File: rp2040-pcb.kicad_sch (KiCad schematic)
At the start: 43 parts, among them J1 Conn_01x20_Male, J2 Conn_01x20_Male, J3 USB_C_Receptacle, SW1 SW_Push, SW2 SW_Push, U1 TPS54202DDC, U2 W25Q128JVS, U3 RP2040, Y1 Crystal_GND24

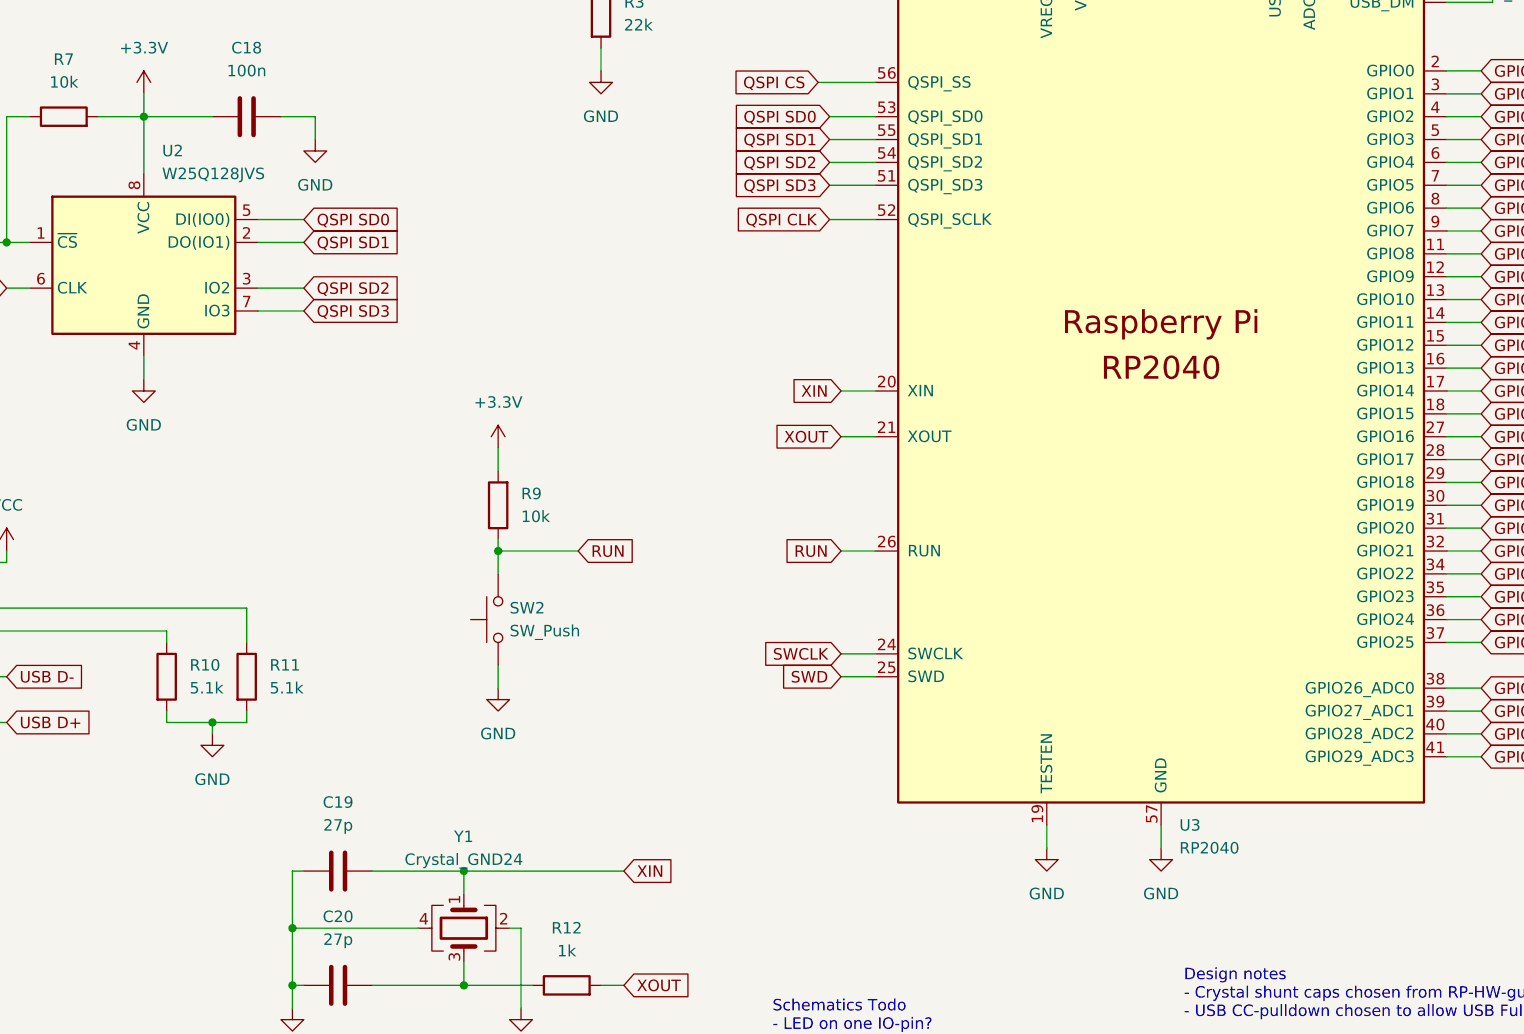
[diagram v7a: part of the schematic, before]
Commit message: Added footprints to all components.
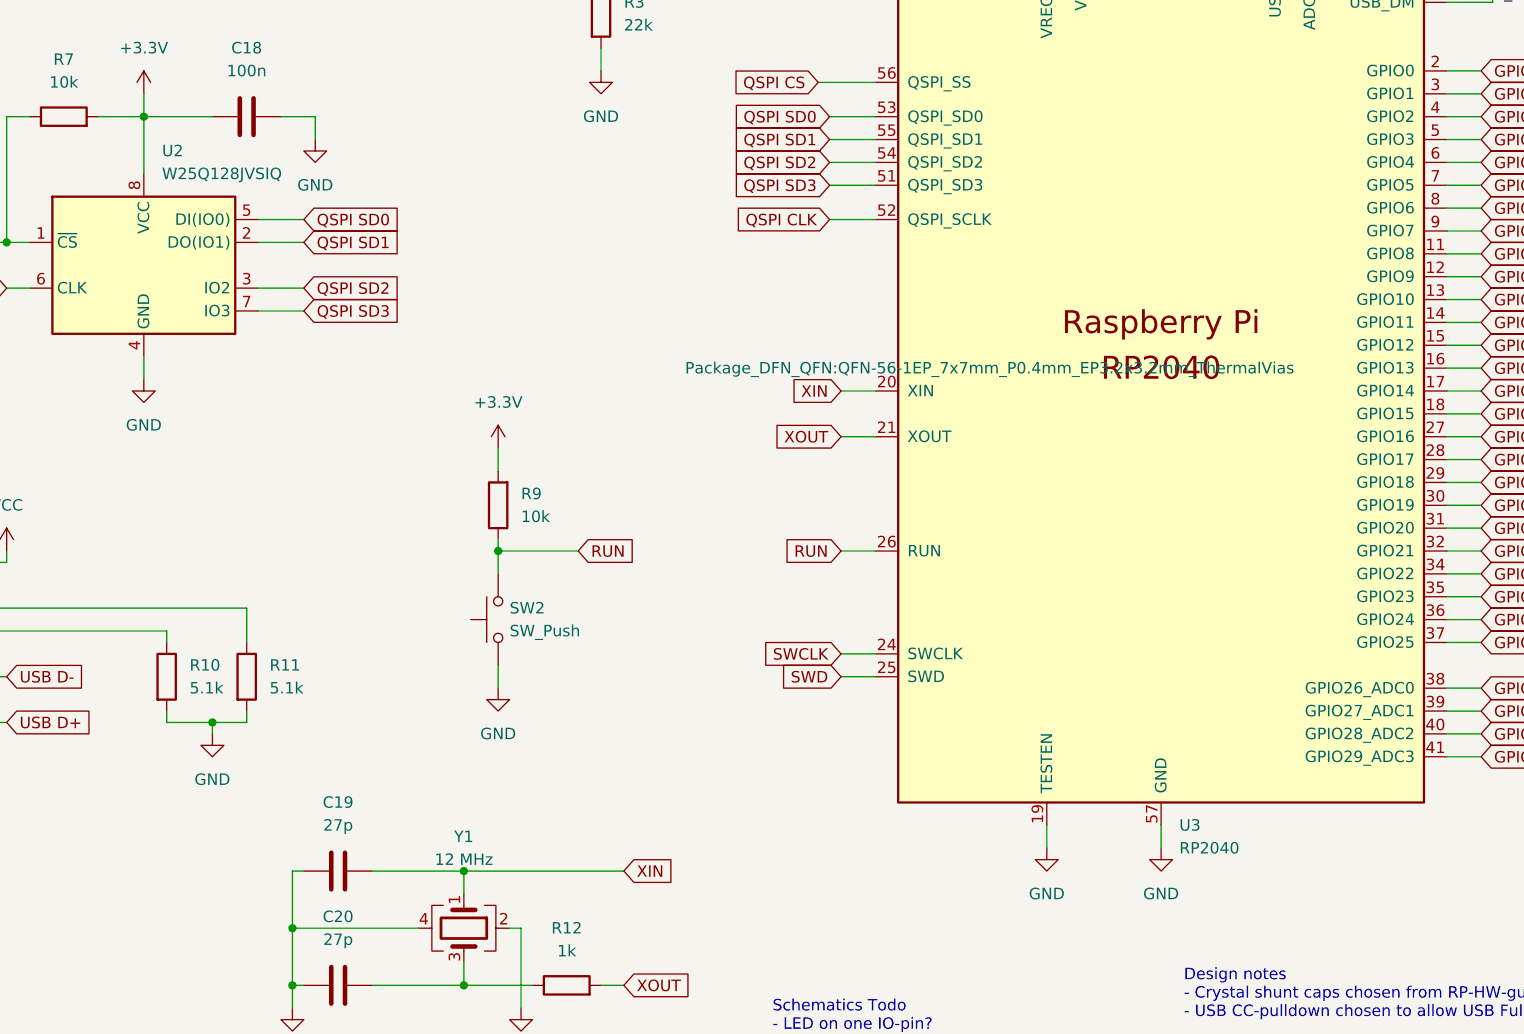
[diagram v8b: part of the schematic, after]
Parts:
- C1, C10, C9: footprint Capacitor_SMD:C_0805_2012Metric -> Capacitor_SMD:C_0603_1608Metric
- C11, C12, C13, C14, C15, C16, C17, C18, C19, C2, C20, C3, C6, C7, C8: footprint Capacitor_SMD:C_0805_2012Metric -> Capacitor_SMD:C_0402_1005Metric
- J1, J2: footprint (none) -> Connector_PinHeader_2.54mm:PinHeader_1x20_P2.54mm_Vertical
- J3: footprint (none) -> Connector_USB:USB_C_Receptacle_Palconn_UTC16-G
- L1: footprint (none) -> Inductor_SMD:L_0603_1608Metric
- PWR_LED1: footprint (none) -> LED_SMD:LED_0805_2012Metric
- R1, R10, R11, R12, R2, R3, R4, R5, R6, R7, R8, R9: footprint (none) -> Resistor_SMD:R_0402_1005Metric
- SW1, SW2: footprint (none) -> Button_Switch_SMD:SW_SPST_TL3342
- U2: value W25Q128JVS -> W25Q128JVSIQ
- U3: footprint RP2040_minimal:RP2040-QFN-56 -> Package_DFN_QFN:QFN-56-1EP_7x7mm_P0.4mm_EP3.2x3.2mm_ThermalVias
- Y1: value Crystal_GND24 -> 12 MHz; footprint (none) -> Oscillator:Oscillator_SMD_EuroQuartz_XO32-4Pin_3.2x2.5mm; Name (none) -> XL2EL89CSI-111YLC-12M
